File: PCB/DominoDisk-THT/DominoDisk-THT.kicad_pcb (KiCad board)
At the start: 2 copper layers, 45.7 x 38.9 mm, 18 parts, among them J2 MicroSD module, J3 UART, J4 Daisy port out, J5 Daisy port in, U1 PC817

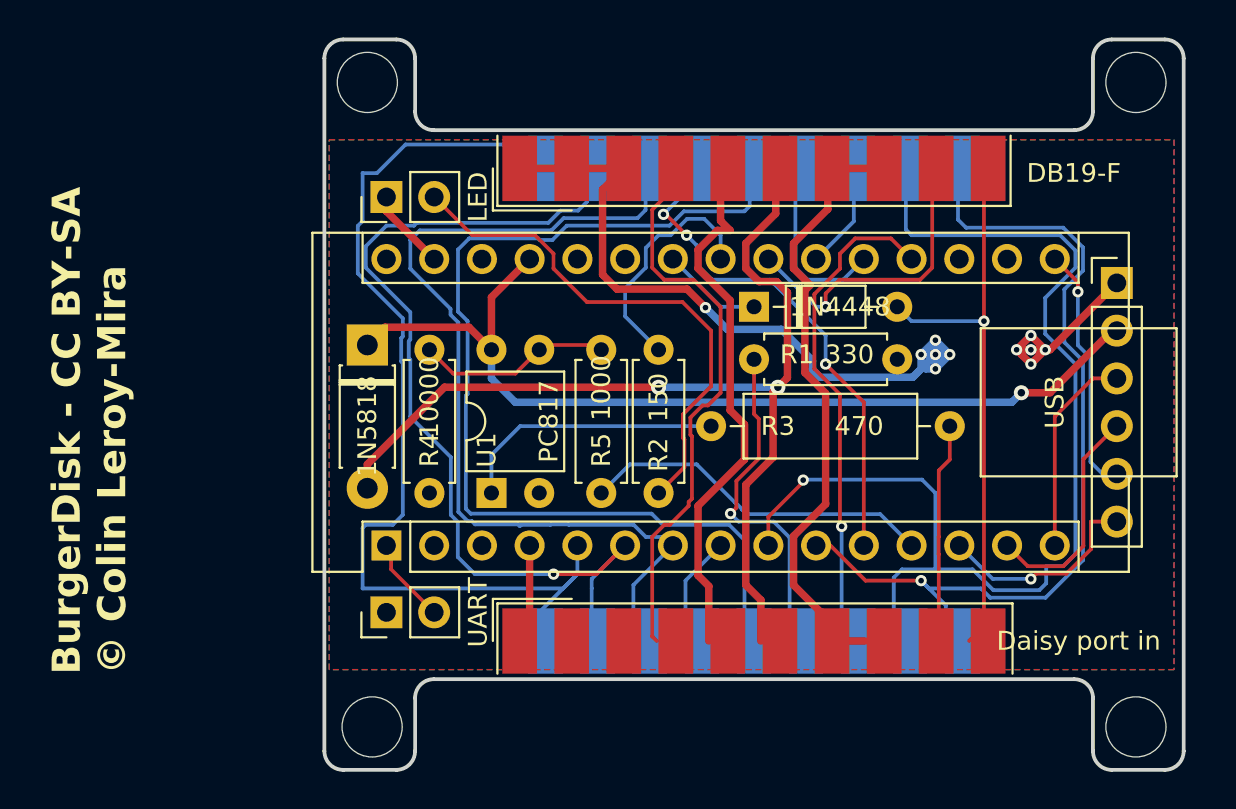
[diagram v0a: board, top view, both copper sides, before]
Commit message: Renames, move to resonator on Domino
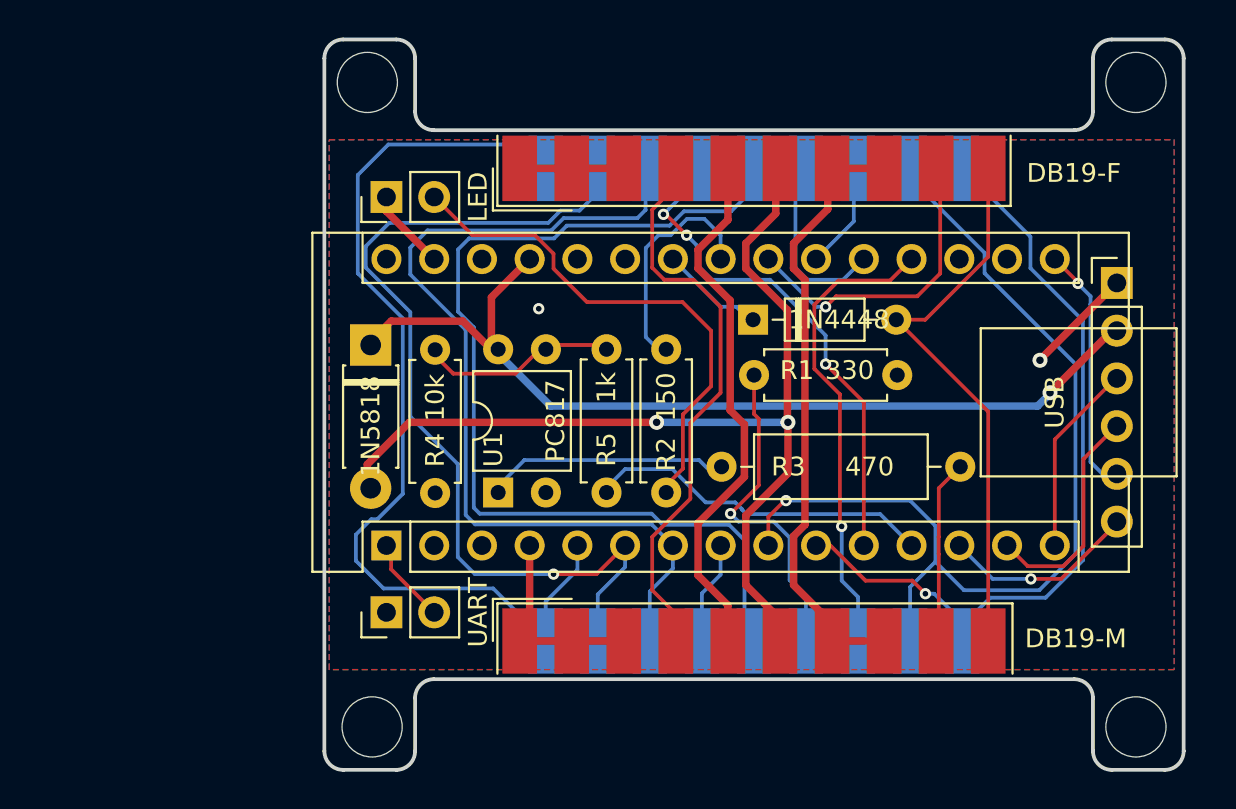
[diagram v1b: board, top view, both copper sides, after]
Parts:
- J2: value MicroSD module -> GND-MicroSD module
- R4: value 10000 -> 10k
- R5: value 1000 -> 1k
- moved R3 2.23 mm to (111.0, 71.2)
- moved R1 0.84 mm to (107.7, 66.4)
- moved D2 0.69 mm to (100.0, 63.4)
- moved R2 0.41 mm to (95.4, 72.6)
- moved U1 0.36 mm to (86.5, 72.6)
- moved R4 0.30 mm to (83.1, 72.6)
- moved R5 0.28 mm to (92.2, 72.6)
- moved D3 0.18 mm to (79.7, 64.8)
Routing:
- net GND: track 63.0 -> 26.5 mm, vias 11 -> 2
- net RDDATA: track 61.0 -> 51.0 mm
- net WRDATA: track 47.5 -> 42.7 mm
- net PH0: track 53.8 -> 51.6 mm
- net DRV2_in: track 11.7 -> 9.81 mm
- net WREQ: track 53.8 -> 52.2 mm
- net DRV1_in: track 26.4 -> 25.0 mm
- net +12V: track 33.0 -> 31.9 mm
- net Net-(R3-Pad2): track 14.3 -> 13.3 mm
- net PH2: track 49.3 -> 48.4 mm
- net CS: track 11.2 -> 10.4 mm
- net MISO: track 11.0 -> 10.3 mm
- net HDSEL_in: track 18.2 -> 17.6 mm
- net Net-(A1-A4): track 12.9 -> 12.3 mm
- net WRPROT_out: track 30.5 -> 30.1 mm, vias 1 -> 0
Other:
- board text removed: "BurgerDisk - CC BY-SA © Colin Leroy-Mira"

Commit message: Cleanup PCBs, fatter power traces
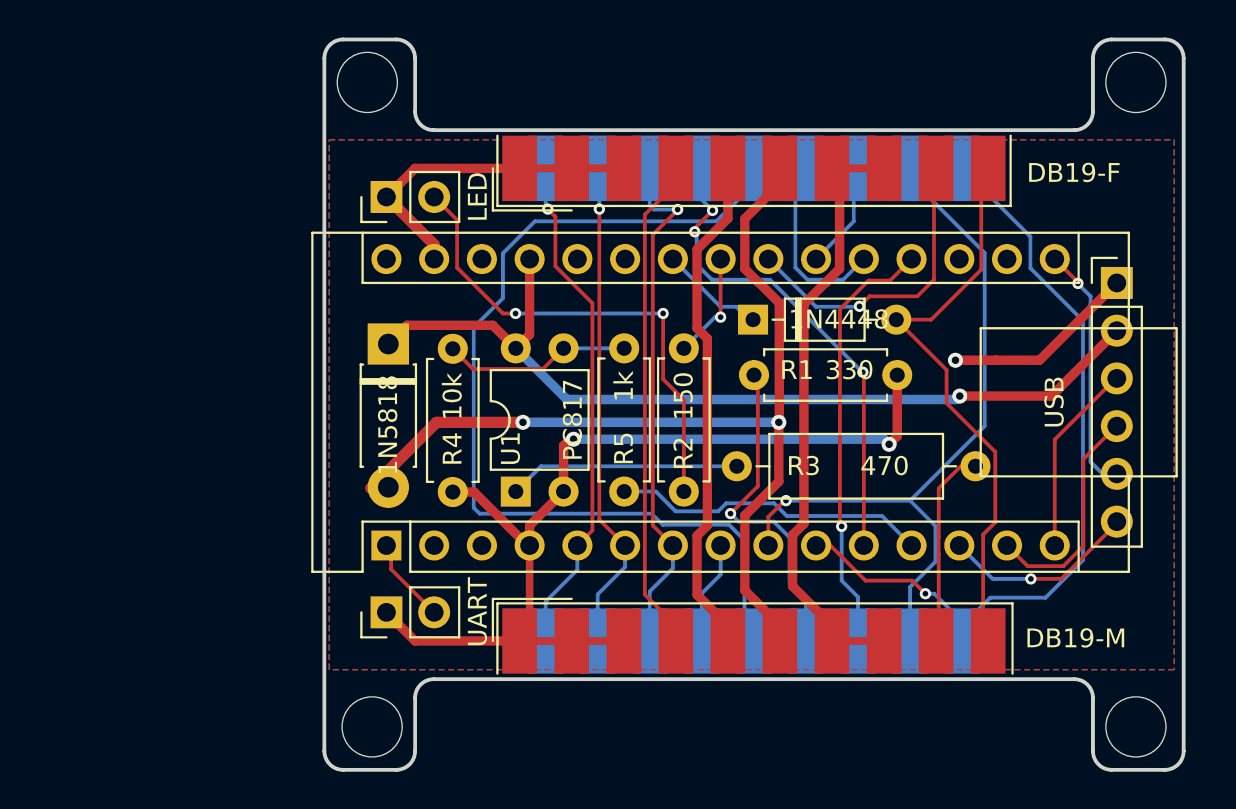
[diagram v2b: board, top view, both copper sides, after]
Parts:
- moved D3 0.94 mm to (80.6, 64.7)
- moved R2 0.94 mm to (96.3, 72.6)
- moved R4 0.94 mm to (84.0, 72.6)
- moved R5 0.94 mm to (93.2, 72.6)
- moved U1 0.94 mm to (87.4, 72.6)
- moved R3 0.81 mm to (111.9, 71.2)
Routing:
- net GND: track 26.5 -> 78.4 mm, vias 2 -> 3
- net PH0: track 51.6 -> 27.2 mm, vias 0 -> 1
- net PH1: track 49.0 -> 26.2 mm
- net PH2: track 48.4 -> 28.0 mm, vias 0 -> 1
- net RDDATA: track 51.0 -> 38.4 mm
- net Net-(A1-A4): track 12.3 -> 5.73 mm, vias 0 -> 1
- net EN3.5: track 30.2 -> 24.9 mm
- net 5V_apple2: track 53.2 -> 49.8 mm
- net WREQ: track 52.2 -> 49.0 mm
- net 5V_burgerDisk: track 50.4 -> 47.4 mm
- net -12V: track 28.5 -> 26.1 mm
- net DRV1_in: track 25.0 -> 23.0 mm
- net WRDATA: track 42.7 -> 40.8 mm
- net DRV2_burgerDisk: track 18.6 -> 16.8 mm
- net Net-(D4-A): track 27.7 -> 26.2 mm, vias 0 -> 2
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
